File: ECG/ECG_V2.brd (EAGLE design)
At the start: 69.9 x 35.6 mm, 32 parts, among them J1 TC2030-CTX-NL, U1 AD8232, U4 BGM111-VISUAL-A

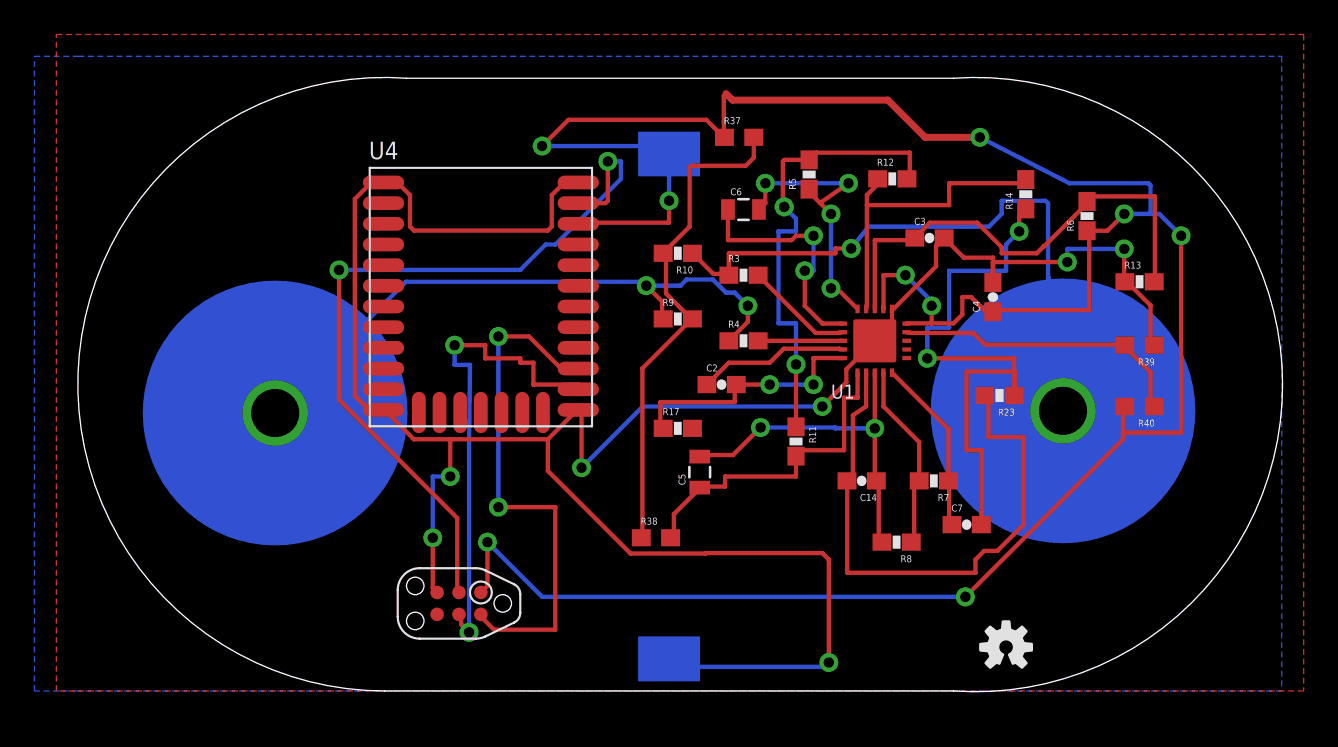
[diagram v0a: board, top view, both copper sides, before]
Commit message: Added new tag connect component and corrected pin configuation
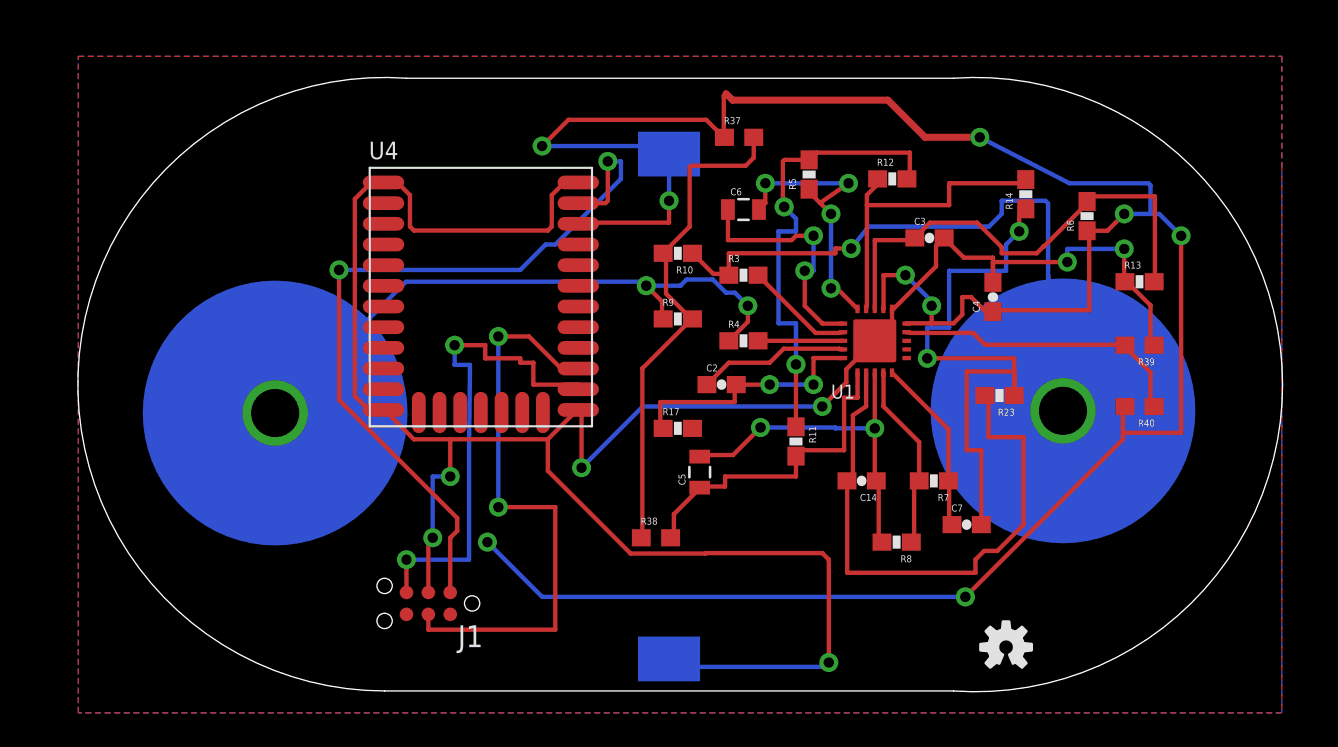
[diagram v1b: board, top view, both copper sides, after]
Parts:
- J1: value TC2030-CTX-NL -> (none); device tag_connector:TC2030-IDC-NL -> tag-connect:TC2030-MCP-NL
- moved J1 0.76 mm to (27.9, 34.3)
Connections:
- removed net N$36: J1.2, U4.PF1
- removed net N$37: J1.4, U4.PF0
- new net N$2: J1.5, U4.PF0
- new net N$6: J1.4, U4.PF1
- new net VDD: J1.2
- net 3.3V: no longer J1.1
- net GND: now also J1.3; no longer J1.5
- net N$38: now also J1.1; no longer J1.3
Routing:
- net N$6: track 0.00 -> 34.0 mm, vias 0 -> 2
- net N$36: track 30.5 -> 0.00 mm, vias 2 -> 0
- net N$2: track 0.00 -> 28.6 mm, vias 0 -> 2
- net N$37: track 28.6 -> 0.00 mm, vias 2 -> 0
- net 3.3V: track 151.1 -> 148.0 mm

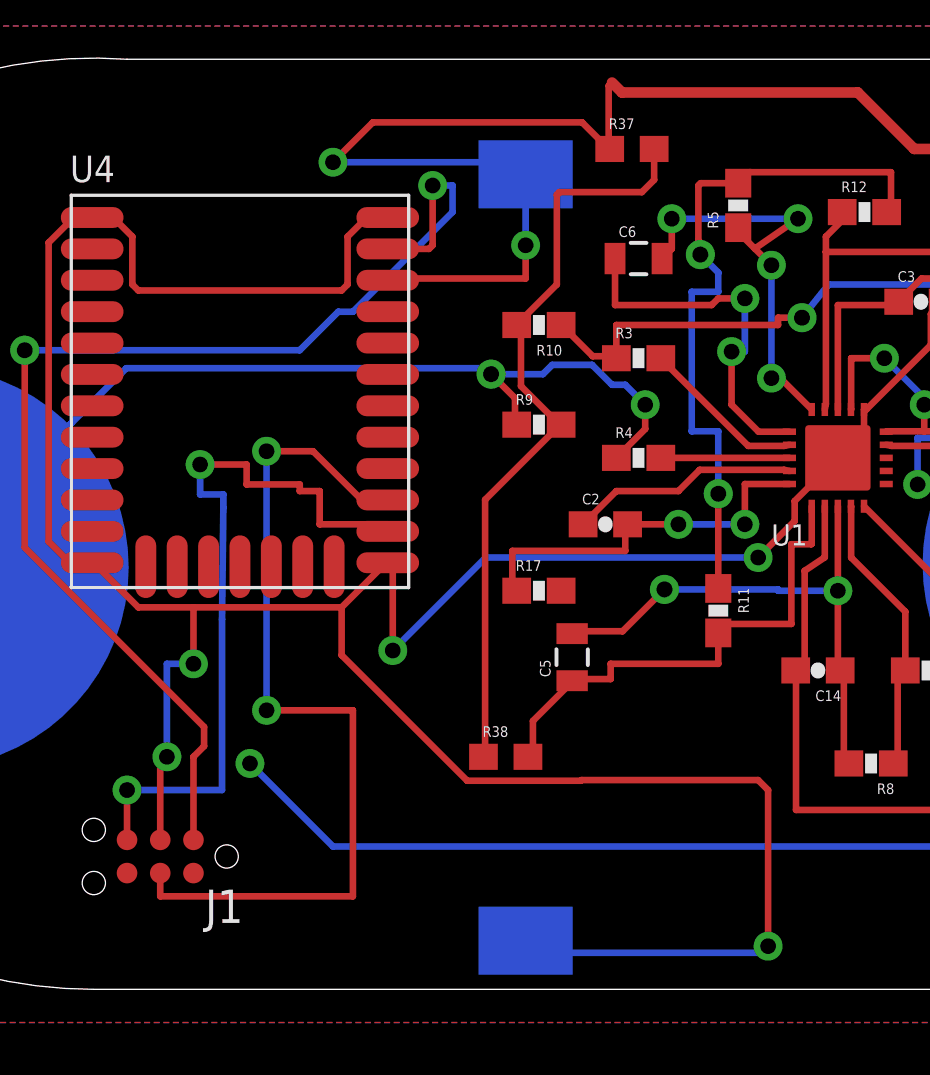
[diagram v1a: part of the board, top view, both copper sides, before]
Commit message: Corrected the Supply issue with tag connect and changed width of some routes
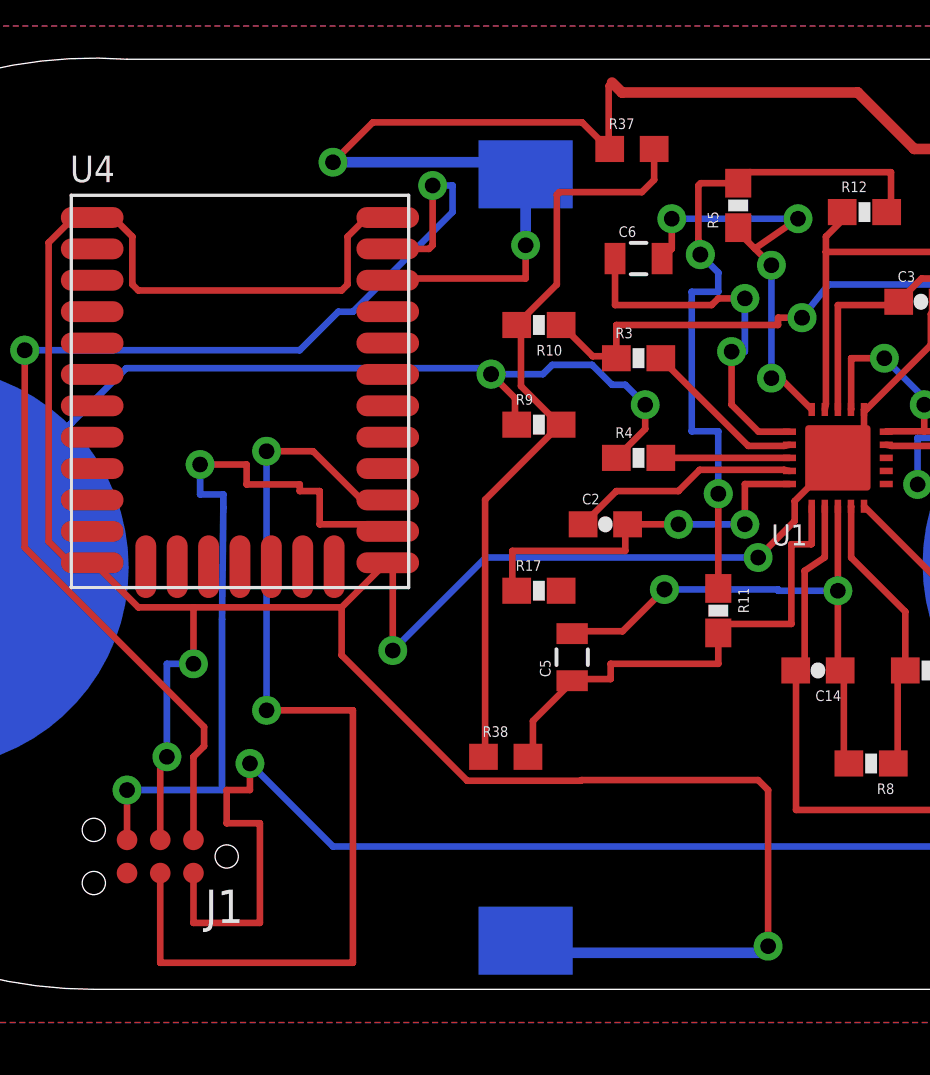
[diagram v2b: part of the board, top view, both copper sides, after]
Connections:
- removed net VDD: J1.2
- net 3.3V: now also J1.2
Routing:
- net 3.3V: track 148.0 -> 160.7 mm
- net N$6: track 34.0 -> 39.1 mm
- net GND: track 142.4 -> 142.9 mm
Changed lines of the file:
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@@
 <via x="48.641" y="30.861" extent="1-16" drill="0.6"/>
 <wire x1="48.641" y1="30.861" x2="48.387" y2="30.607" width="0.254" layer="16"/>
-<wire x1="48.387" y1="30.607" x2="40.386" y2="30.607" width="0.254" layer="16"/>
 <wire x1="40.386" y1="30.607" x2="39.923" y2="31.07" width="0.254" layer="16"/>
 <wire x1="39.923" y1="31.07" x2="39.37" y2="31.07" width="0.254" layer="16"/>
@@
 <vertex x="5.08" y="27.94"/>
 </polygon>
+<wire x1="40.386" y1="30.607" x2="48.641" y2="30.607" width="0.4064" layer="16"/>
+<wire x1="48.641" y1="30.607" x2="48.641" y2="30.861" width="0.4064" layer="16"/>
 </signal>
 <signal name="SIGNAL_OUT">
@@
 <wire x1="39.37" y1="56.388" x2="39.37" y2="57.658" width="0.254" layer="1"/>
 <via x="39.37" y="57.658" extent="1-16" drill="0.6"/>
-<wire x1="39.37" y1="57.658" x2="39.37" y2="60.37" width="0.254" layer="16"/>
 <wire x1="39.37" y1="60.37" x2="38.907" y2="60.833" width="0.254" layer="16"/>
-<wire x1="38.907" y1="60.833" x2="32.004" y2="60.833" width="0.254" layer="16"/>
 <via x="32.004" y="60.833" extent="1-16" drill="0.6"/>
 <wire x1="32.004" y1="60.833" x2="33.528" y2="62.357" width="0.254" layer="1"/>
@@
 <wire x1="52.07" y1="63.5" x2="54.229" y2="61.341" width="0.4064" layer="1"/>
 <wire x1="54.229" y1="61.341" x2="57.404" y2="61.341" width="0.4064" layer="1"/>
+<contactref element="J1" pad="2"/>
+<wire x1="26.67" y1="33.655" x2="26.67" y2="31.75" width="0.254" layer="1"/>
+<wire x1="26.67" y1="31.75" x2="29.21" y2="31.75" width="0.254" layer="1"/>
+<wire x1="29.21" y1="31.75" x2="29.21" y2="35.56" width="0.254" layer="1"/>
+<wire x1="29.21" y1="35.56" x2="27.94" y2="35.56" width="0.254" layer="1"/>
+<wire x1="27.94" y1="35.56" x2="27.94" y2="36.83" width="0.254" layer="1"/>
+<wire x1="27.94" y1="36.83" x2="28.829" y2="36.83" width="0.254" layer="1"/>
+<wire x1="28.829" y1="36.83" x2="28.829" y2="37.846" width="0.254" layer="1"/>
+<wire x1="32.004" y1="60.833" x2="38.907" y2="60.833" width="0.4064" layer="16"/>
+<wire x1="39.37" y1="60.37" x2="39.37" y2="57.658" width="0.4064" layer="16"/>
 </signal>
 <signal name="LA">
@@
 <wire x1="26.67" y1="38.1" x2="26.67" y2="34.925" width="0.254" layer="1"/>
 </signal>
-<signal name="VDD">
-<contactref element="J1" pad="2"/>
-</signal>
 <signal name="N$2">
 <contactref element="U4" pad="PF0"/>
@@
 <signal name="N$6">
 <contactref element="U4" pad="PF1"/>
-<wire x1="32.766" y1="32.766" x2="32.766" y2="39.878" width="0.254" layer="1"/>
+<wire x1="32.766" y1="30.226" x2="32.766" y2="39.878" width="0.254" layer="1"/>
 <wire x1="32.766" y1="39.878" x2="29.464" y2="39.878" width="0.254" layer="1"/>
 <via x="29.464" y="39.878" extent="1-16" drill="0.6"/>
@@
 <wire x1="33.614" y1="47.92" x2="34.098" y2="47.92" width="0.254" layer="1"/>
 <contactref element="J1" pad="4"/>
-<wire x1="32.766" y1="32.766" x2="25.4" y2="32.766" width="0.254" layer="1"/>
-<wire x1="25.4" y1="32.766" x2="25.4" y2="33.655" width="0.254" layer="1"/>
+<wire x1="32.766" y1="30.226" x2="25.4" y2="30.226" width="0.254" layer="1"/>
+<wire x1="25.4" y1="30.226" x2="25.4" y2="33.655" width="0.254" layer="1"/>
 </signal>
 </signals>
